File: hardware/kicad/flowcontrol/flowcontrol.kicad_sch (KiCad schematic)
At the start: 17 parts, among them J1 SOL1_PORT, J2 SOL2_PORT, Q1 SOL1_NPN, Q2 SOL2_NPN, SW1 SOL1_MASTER, SW2 SOL2_MASTER, SW3 SOL1_DURA, SW4 SOL1_DELAY, SW5 SOL2_DURA, SW6 SOL2_DELAY, U1 SOL1_DISP, U2 SOL2_DISP

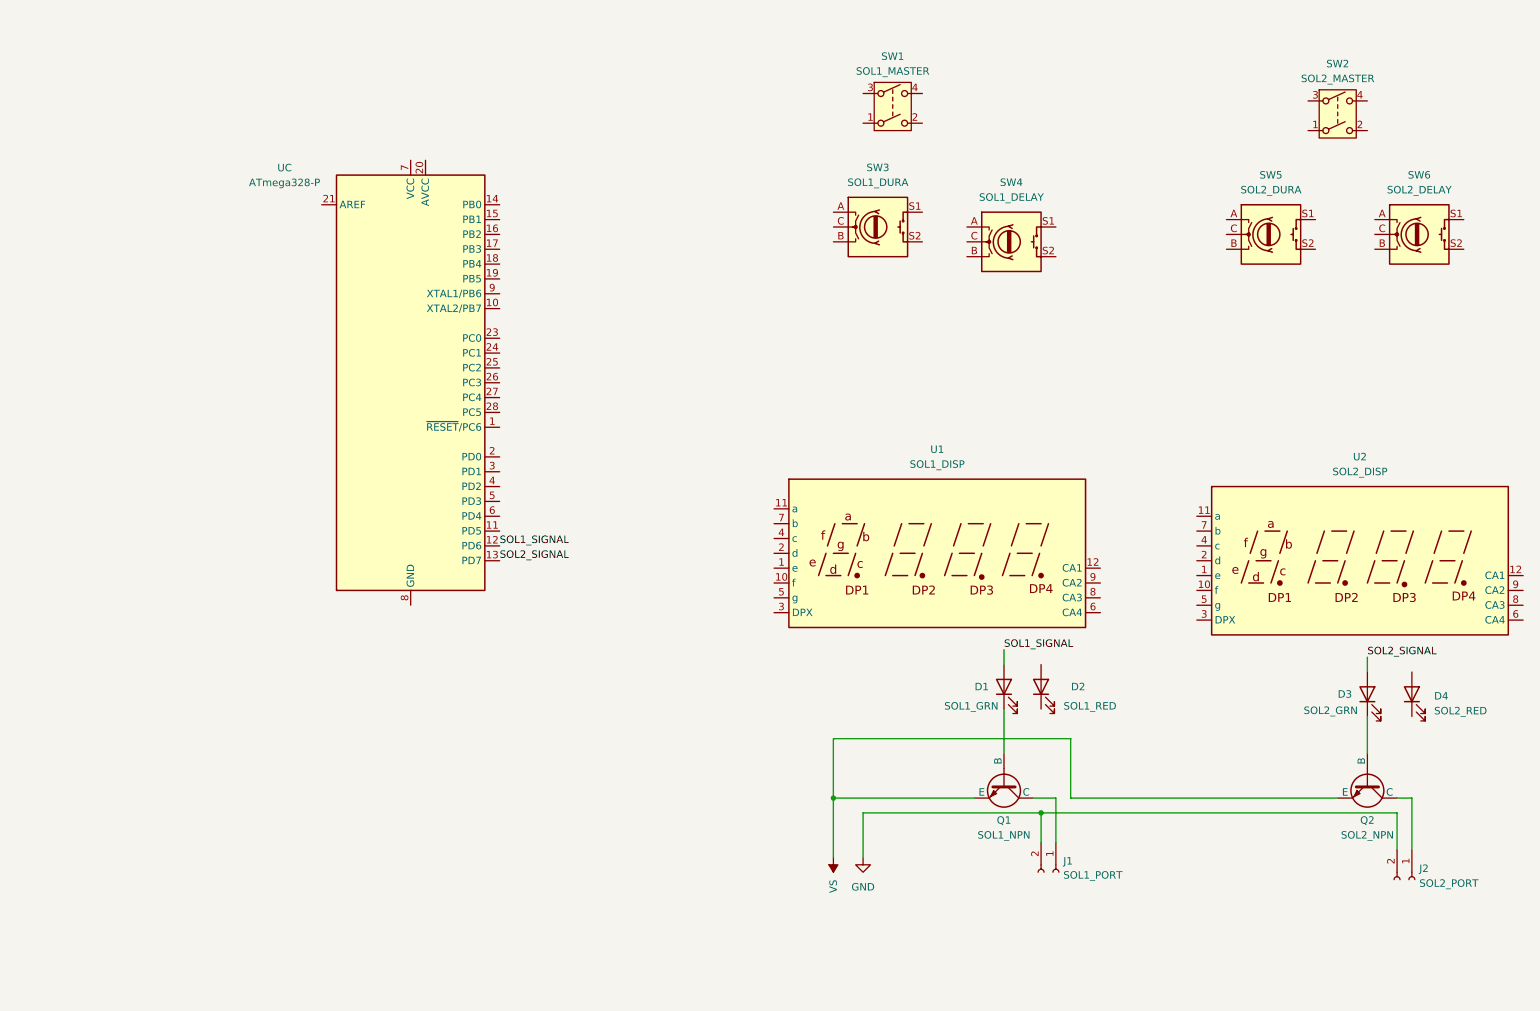
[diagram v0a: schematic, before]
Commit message: updated kicad file
connected most devices together through labels.
still requires LCD I2C modules or 4-digit schematic blocks.
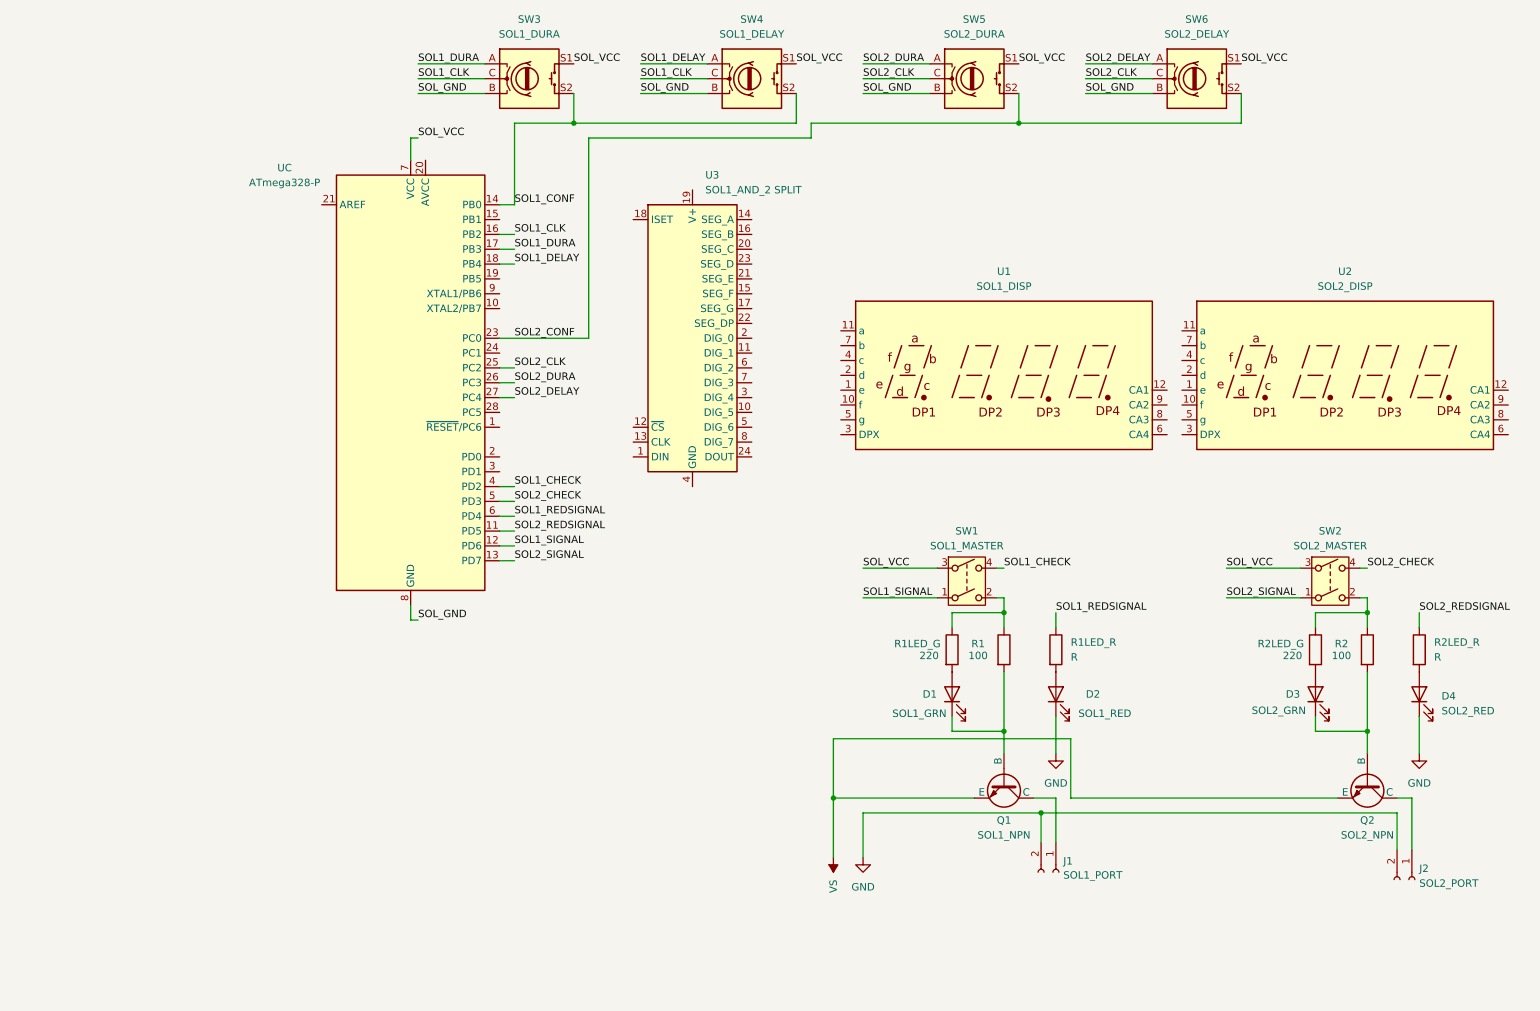
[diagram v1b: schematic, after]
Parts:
- added R1, R2: 100, symbol Device:R
- added R1LED_G, R2LED_G: 220, symbol Device:R
- added R1LED_R, R2LED_R: R, symbol Device:R
- added U3: SOL1_AND_2 SPLIT, Package_DIP:DIP-24_W7.62mm, symbol Driver_LED:MAX7221xNG
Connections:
- net GND: now also D2.1 (K), D4.1 (K)
- net SOL1_SIGNAL: now also SW1.1; no longer D1.2 (A)
- net SOL2_SIGNAL: now also SW2.1; no longer D3.2 (A)
- net at D3.1 (K), Q2.2 (B): now also R2.2
- net SOL1_DELAY: now reaches SW4.A
- net SOL1_DELAY: now also UC.18 (PB4)
- net SOL_GND: now reaches SW4.B
- net SOL_GND: now also SW3.B, SW5.B, SW6.B, UC.22 (GND), UC.8 (GND)
- net SOL1_CLK: now reaches SW4.C
- net SOL1_CLK: now also SW3.C, UC.16 (PB2)
- net SOL_VCC: now reaches SW4.S1
- net SOL_VCC: now also SW1.3, SW2.3, SW3.S1, SW5.S1, SW6.S1, UC.7 (VCC)
- net SOL1_CONF: now reaches SW4.S2
- net SOL1_CONF: now also SW3.S2, UC.14 (PB0)
- net at SW2.2: now also R2.1, R2LED_G.1
- net SOL2_CHECK: now reaches SW2.4
- net SOL2_CHECK: now also UC.5 (PD3)
- net at SW1.2: now also R1.1, R1LED_G.1
- net SOL1_CHECK: now reaches SW1.4
- net SOL1_CHECK: now also UC.4 (PD2)
- net at D4.2 (A): now also R2LED_R.2
- net SOL2_DELAY: now reaches SW6.A
- net SOL2_DELAY: now also UC.27 (PC4)
- net SOL2_CLK: now reaches SW6.C
- net SOL2_CLK: now also SW5.C, UC.25 (PC2)
- net SOL2_CONF: now reaches SW6.S2
- net SOL2_CONF: now also SW5.S2, UC.23 (PC0)
- net at D2.2 (A): now also R1LED_R.2
- net SOL2_DURA: now reaches SW5.A
- net SOL2_DURA: now also UC.26 (PC3)
- net SOL1_DURA: now reaches SW3.A
- net SOL1_DURA: now also UC.17 (PB3)
- net at D1.1 (K), Q1.2 (B): now also R1.2
- net SOL2_REDSIGNAL: now reaches UC.11 (PD5)
- net SOL2_REDSIGNAL: now also R2LED_R.1
- net SOL1_REDSIGNAL: now reaches UC.6 (PD4)
- net SOL1_REDSIGNAL: now also R1LED_R.1
- new net: D3.2 (A), R2LED_G.2
- new net: D1.2 (A), R1LED_G.2
- new net: U3.4 (GND), U3.9 (GND)
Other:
- moved on the sheet: D1, D2, D3, D4, SW1, SW2, SW3, SW4, SW5, SW6, U1, U2

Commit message: KiCad Sectioning
Turned the schematic into multiple sections - microcontroller, inputs, outputs, and display as the core blocks.
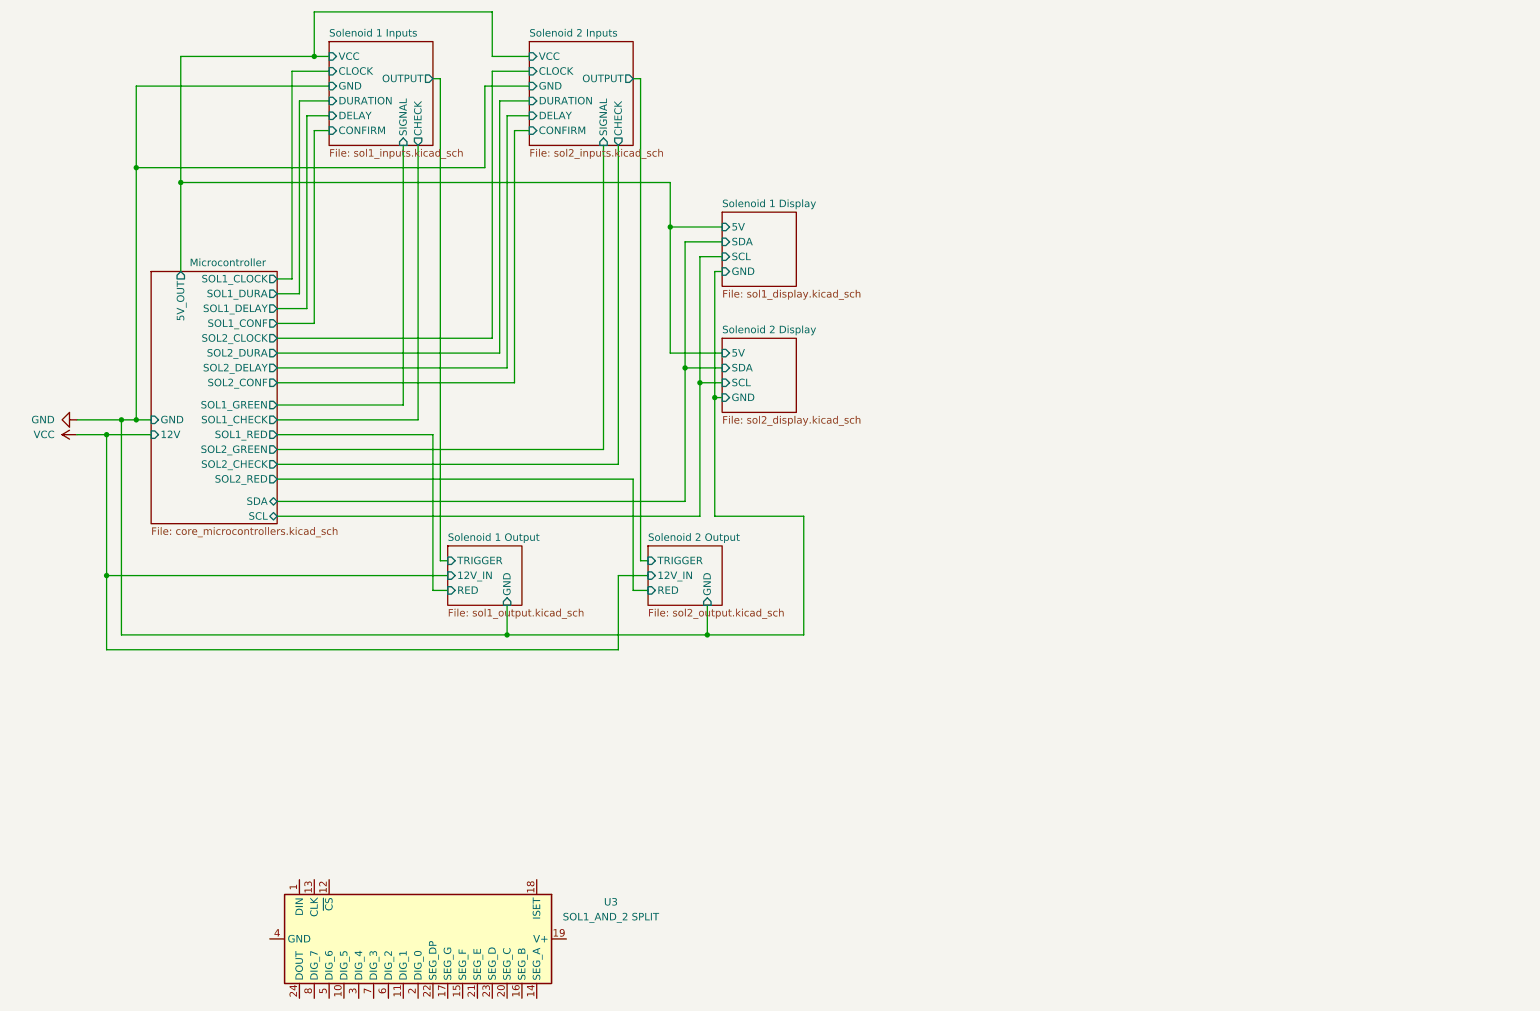
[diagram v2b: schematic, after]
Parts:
- removed D1: SOL1_GRN, symbol Device:LED
- removed D2: SOL1_RED, symbol Device:LED
- removed D3: SOL2_GRN, symbol Device:LED
- removed D4: SOL2_RED, symbol Device:LED
- removed J1: SOL1_PORT, symbol Connector:Conn_01x02_Socket
- removed J2: SOL2_PORT, symbol Connector:Conn_01x02_Socket
- removed Q1: SOL1_NPN, symbol Simulation_SPICE:NPN
- removed Q2: SOL2_NPN, symbol Simulation_SPICE:NPN
- removed R1, R2: 100, symbol Device:R
- removed R1LED_G, R2LED_G: 220, symbol Device:R
- removed R1LED_R, R2LED_R: R, symbol Device:R
- removed SW1: SOL1_MASTER, symbol Switch:SW_DPST
- removed SW2: SOL2_MASTER, symbol Switch:SW_DPST
- removed SW3: SOL1_DURA, symbol Device:RotaryEncoder_Switch
- removed SW4: SOL1_DELAY, symbol Device:RotaryEncoder_Switch
- removed SW5: SOL2_DURA, symbol Device:RotaryEncoder_Switch
- removed SW6: SOL2_DELAY, symbol Device:RotaryEncoder_Switch
- removed U1: SOL1_DISP, Display_7Segment:CA56-12SRWA, symbol Display_Character:CA56-12SRWA
- removed U2: SOL2_DISP, Display_7Segment:CA56-12SRWA, symbol Display_Character:CA56-12SRWA
- removed UC: ATmega328-P, Package_DIP:DIP-28_W7.62mm, symbol MCU_Microchip_ATmega:ATmega328-P
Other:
- added sheet Microcontroller (core_microcontrollers.kicad_sch)
- added sheet Solenoid 1 Display (sol1_display.kicad_sch)
- added sheet Solenoid 1 Inputs (sol1_inputs.kicad_sch)
- added sheet Solenoid 1 Output (sol1_output.kicad_sch)
- added sheet Solenoid 2 Display (sol2_display.kicad_sch)
- added sheet Solenoid 2 Inputs (sol2_inputs.kicad_sch)
- added sheet Solenoid 2 Output (sol2_output.kicad_sch)
- title: (none) -> 3/4" Garden Pipe Flow Controller
- moved on the sheet: U3

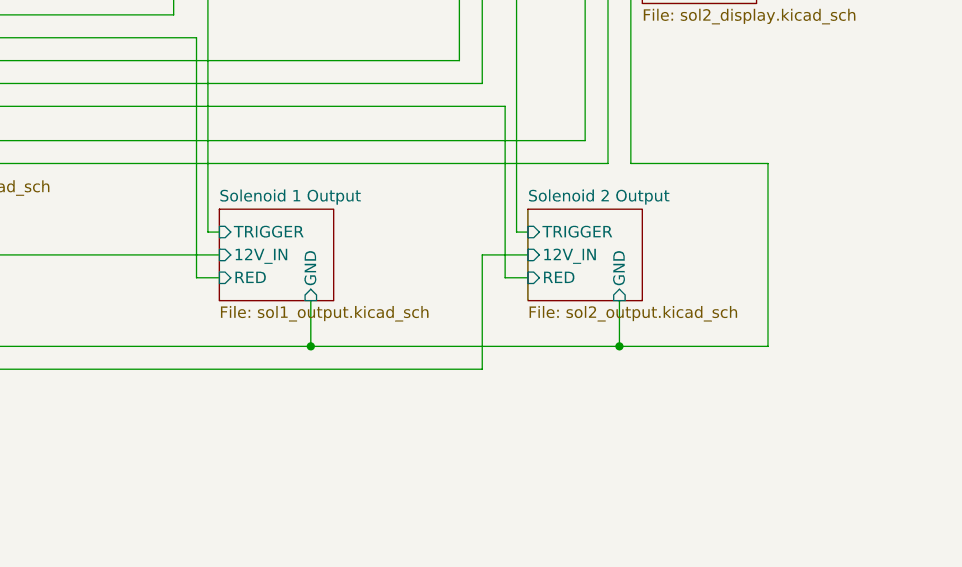
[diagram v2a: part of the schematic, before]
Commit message: Added requested test procedures
Four ideal test protocols have been added:
- Power-up sanity check
- Manual activation
- Small-scale interval
- Individual settings
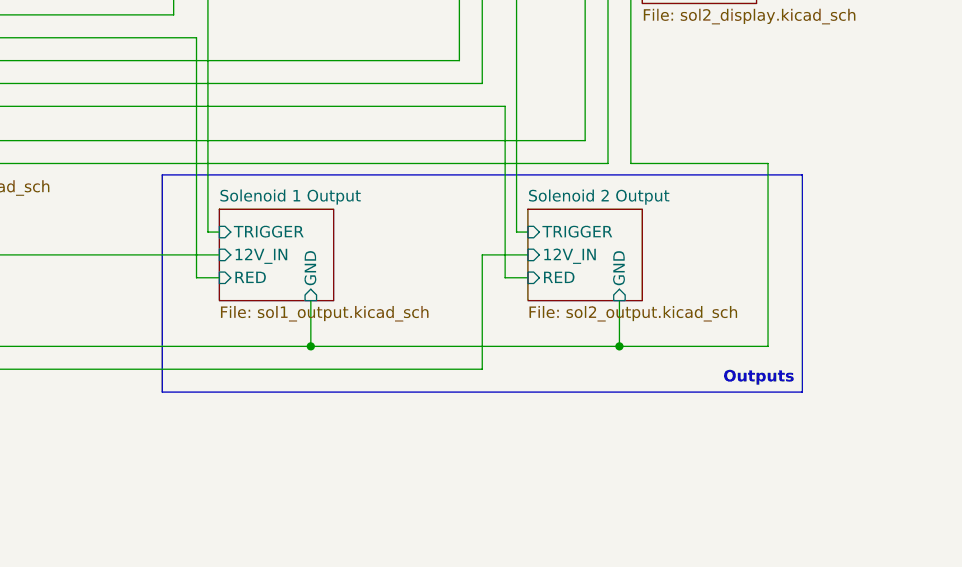
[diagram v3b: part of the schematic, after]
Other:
- note added: "Outputs"
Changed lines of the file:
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@@
+		)
+	)
+	(rectangle
+		(start 81.28 101.6)
+		(end 152.4 125.73)
+		(stroke
+			(width 0.0508)
+			(type solid)
+			(color 10 131 255 1)
+		)
+		(fill
+			(type none)
+		)
+	)
+	(text "Outputs"
+		(exclude_from_sim no)
+		(at 147.574 124.206 0)
+		(effects
+			(font
+				(size 1.27 1.27)
+				(thickness 0.254)
+				(bold yes)
+			)
 		)
 	)

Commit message: Schemiatic update
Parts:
- U3: footprint Package_DIP:DIP-24_W7.62mm -> Package_DIP:DIP-28_W7.62mm
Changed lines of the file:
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@@
 			)
 		)
-		(property "Footprint" "Package_DIP:DIP-24_W7.62mm"
+		(property "Footprint" "Package_DIP:DIP-28_W7.62mm"
 			(at 83.82 171.45 0)
 			(effects

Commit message: Updated KiCad schematic to final rendition
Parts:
- removed U3: SOL1_AND_2 SPLIT, Package_DIP:DIP-28_W7.62mm, symbol Driver_LED:MAX7221xNG
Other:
- sheet Solenoid 1 Inputs renamed Input Display
- removed sheet Solenoid 1 Display
- removed sheet Solenoid 2 Display
- removed sheet Solenoid 2 Inputs
- added sheet Solenoid 3 Output (sol1_output.kicad_sch)
- sheet Input Display ports: added 12V_R, DT, GND_E, GND_R, GND_S, SCL, SDA, SWITCH, VCC_E, VCC_R, VCC_S; removed CHECK, CONFIRM, DELAY, DURATION, GND, OUTPUT, SIGNAL, VCC
- sheet Microcontroller ports: added ENC_A, ENC_B, ENC_SW, SOL1_MAIN, SOL1_OUT, SOL1_SEL, SOL1_WAIT, SOL2_MAIN, SOL2_OUT, SOL2_SEL, SOL2_WAIT, SOL3_MAIN, SOL3_OUT, SOL3_SEL, SOL3_WAIT; removed SOL1_CHECK, SOL1_CLOCK, SOL1_CONF, SOL1_DELAY, SOL1_DURA, SOL1_GREEN, SOL1_RED, SOL2_CHECK, SOL2_CLOCK, SOL2_CONF, SOL2_DELAY, SOL2_DURA, SOL2_GREEN, SOL2_RED
- sheet Solenoid 1 Output ports: added 12V_SUPPLY, 5V, GND_SUPPLY, MAIN, SETTING; removed 12V_IN
- sheet Solenoid 2 Output: file sol2_output.kicad_sch -> sol1_output.kicad_sch
- sheet Solenoid 2 Output ports: added 12V_SUPPLY, 5V, GND_SUPPLY, MAIN, SETTING; removed 12V_IN

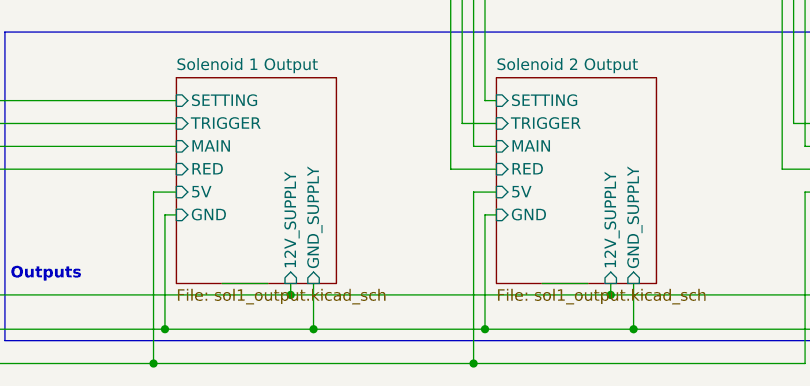
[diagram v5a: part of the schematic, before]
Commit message: labeled the old pcb old
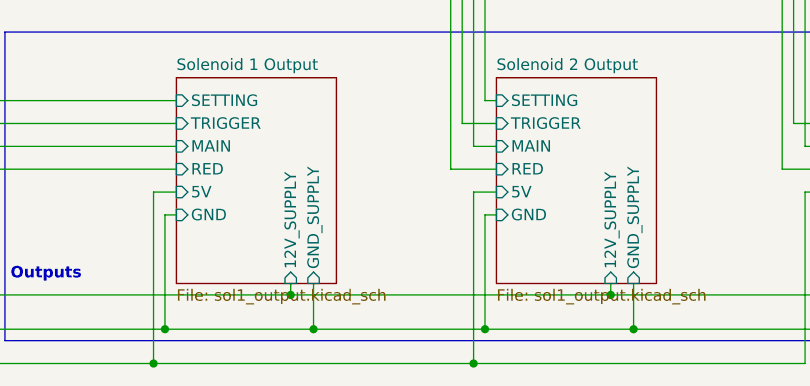
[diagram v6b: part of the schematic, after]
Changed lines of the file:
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@@
-	(wire
-		(pts
-			(xy 107.95 135.89) (xy 102.87 135.89)
-		)
-		(stroke
-			(width 0)
-			(type default)
-		)
-	)
 	(wire
 		(pts
@@
 		)
 		(stroke
-			(width 0)
-			(type default)
-		)
-	)
-	(wire
-		(pts
-			(xy 143.51 135.89) (xy 138.43 135.89)
-		)
-		(stroke
